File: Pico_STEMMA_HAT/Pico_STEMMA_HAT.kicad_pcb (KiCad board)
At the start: 2 copper layers, 58 x 63 mm, 38 parts

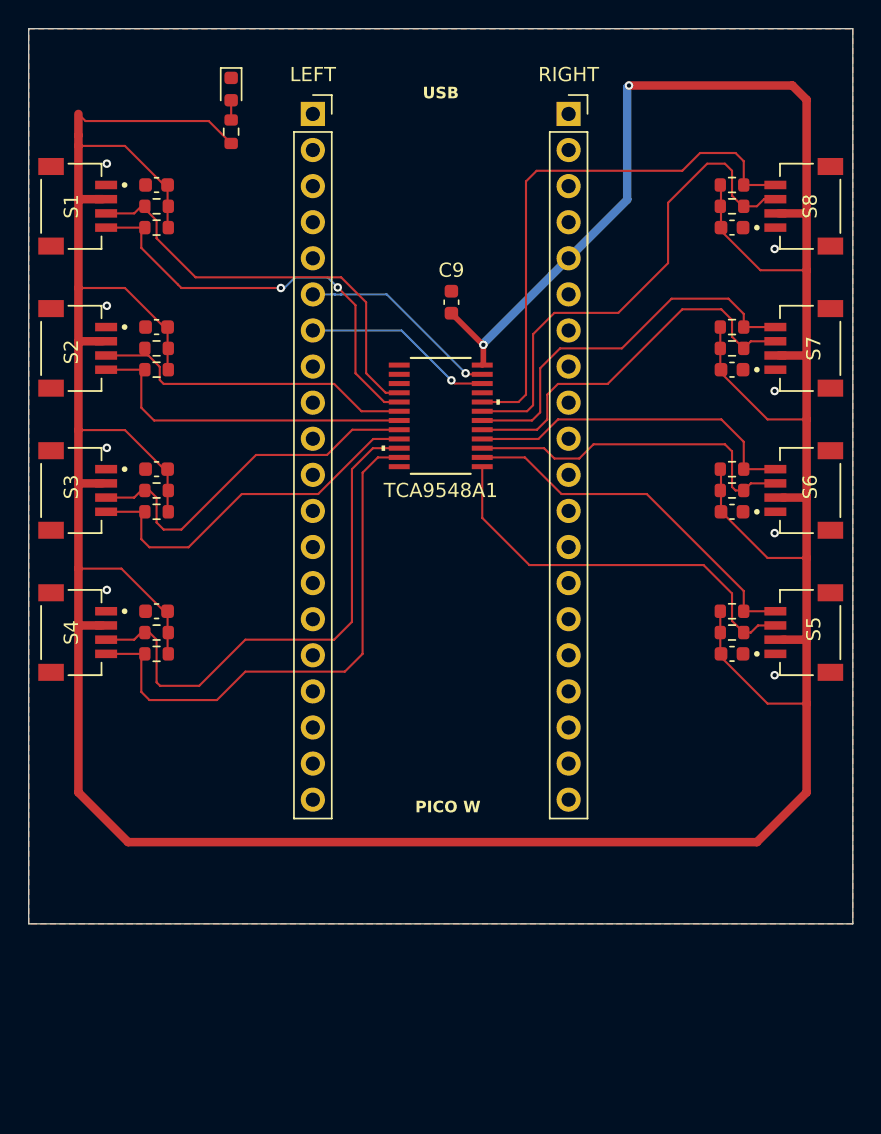
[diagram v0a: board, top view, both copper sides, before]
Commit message: Add GND vias to connect to GND B layer
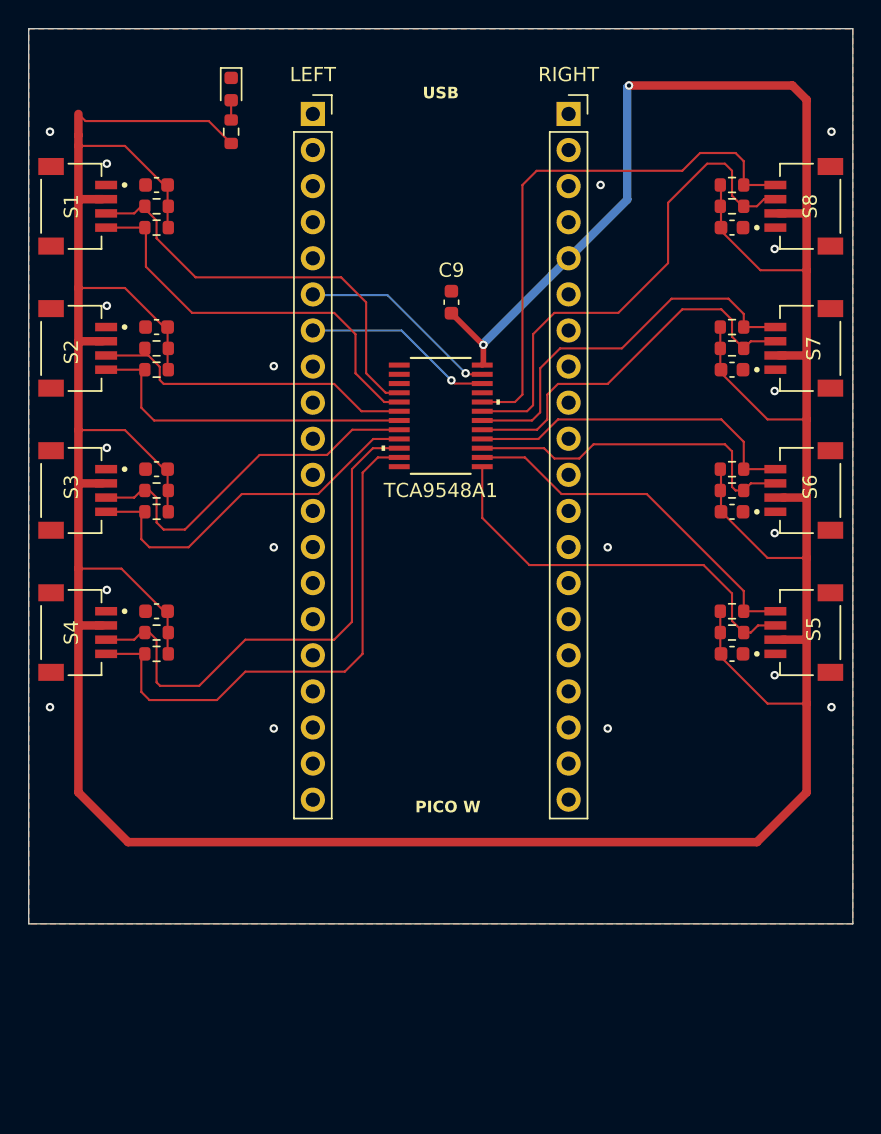
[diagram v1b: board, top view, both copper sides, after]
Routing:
- net /SCL0: track 30.3 -> 29.2 mm, vias 2 -> 0
- net GND: vias 8 -> 18

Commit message: Add SD card reader to PCB design
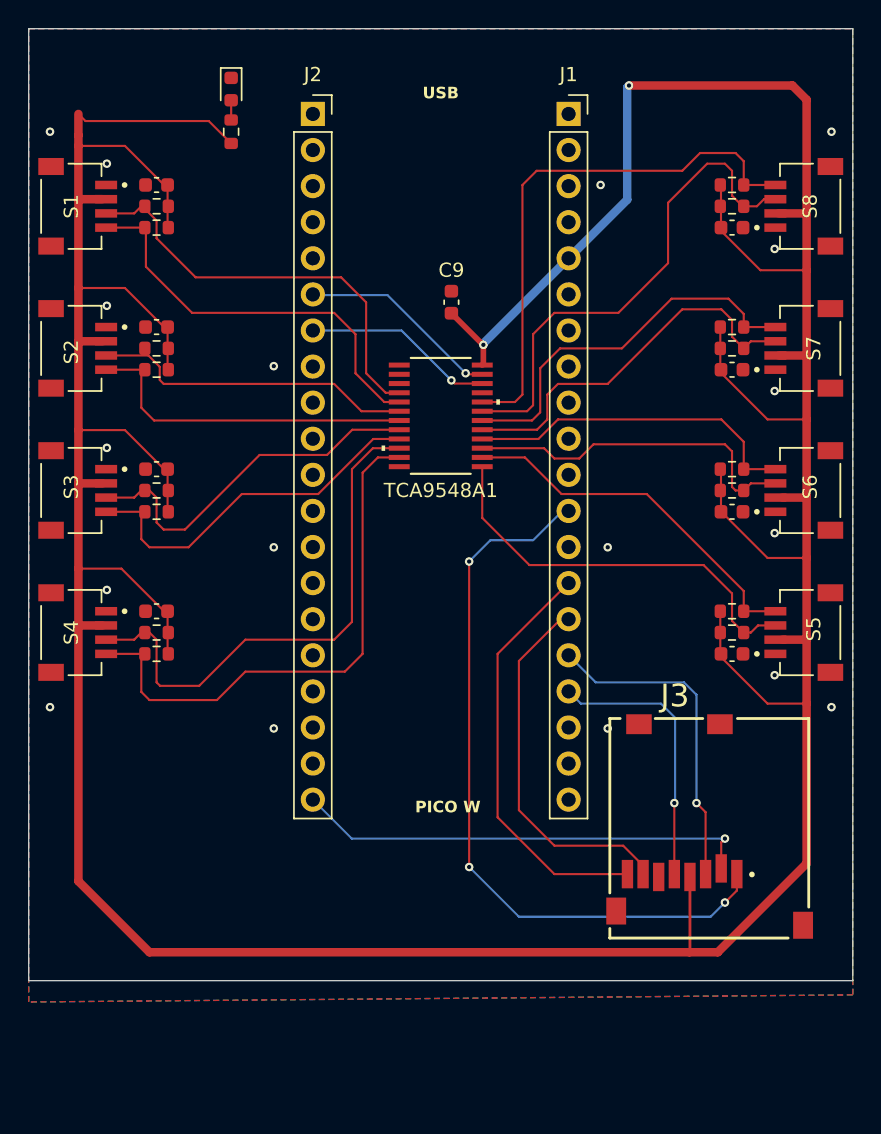
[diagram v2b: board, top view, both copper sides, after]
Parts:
- added J3: SDCARD_MODULE, Pico_Footprints:SDCARD_MODULE_Footprint, F.Cu at (168.9, 128.8)
- renumbered RIGHT to J1, LEFT to J2
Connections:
- net /GPIO16 renamed /GPIO16/DEC
- J1 pad 12: /GPIO22 -> /GPIO22/DAT2
- J1 pad 14: /GPIO21 -> /GPIO21/DAT1
- J1 pad 15: /GPIO20 -> /GPIO20/MISO
- J1 pad 16: /GPIO19 -> /GPIO19/DATA_IN
- J1 pad 17: /GPIO18 -> /GPIO18/SD_CLK
- J2 pad 20: /GPIO15 -> /GPIO15/CS
- S1 pad S1: GND -> (no net)
- S1 pad S2: GND -> (no net)
- S2 pad S1: GND -> (no net)
- S2 pad S2: GND -> (no net)
- S3 pad S1: GND -> (no net)
- S3 pad S2: GND -> (no net)
- S4 pad S1: GND -> (no net)
- S4 pad S2: GND -> (no net)
- S5 pad S1: GND -> (no net)
- S5 pad S2: GND -> (no net)
- S6 pad S1: GND -> (no net)
- S6 pad S2: GND -> (no net)
- S7 pad S1: GND -> (no net)
- S7 pad S2: GND -> (no net)
- S8 pad S1: GND -> (no net)
- S8 pad S2: GND -> (no net)
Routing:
- net /GPIO22/DAT2: track 0.00 -> 52.2 mm, vias 0 -> 3
- net /GPIO15/CS: track 0.00 -> 32.3 mm, vias 0 -> 1
- net /GPIO21/DAT1: track 0.00 -> 29.4 mm
- net /GPIO20/MISO: track 0.00 -> 26.2 mm
- net /GPIO19/DATA_IN: track 0.00 -> 23.0 mm, vias 0 -> 1
- net /GPIO18/SD_CLK: track 0.00 -> 19.3 mm, vias 0 -> 1
- net +3V3: track 299.3 -> 317.6 mm
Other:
- board size 58 x 63 mm -> 58 x 67 mm

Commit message: Add pullup resistors to the SD card reader
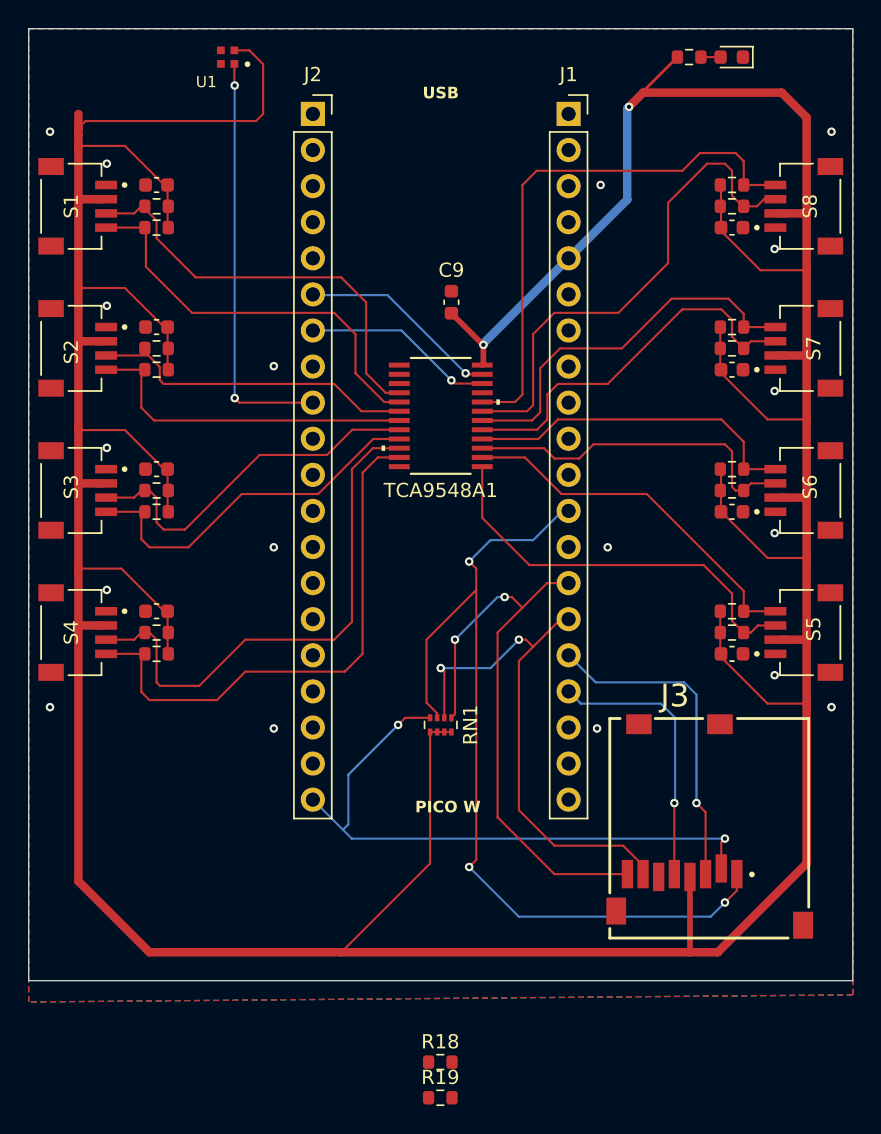
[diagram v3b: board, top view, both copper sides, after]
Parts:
- added R18: 47k, Resistor_SMD:R_0603_1608Metric, F.Cu at (150.0, 145.2)
- added R19: 47k, Resistor_SMD:R_0603_1608Metric, F.Cu at (150.0, 147.7)
- added RN1: 47k, Resistor_SMD:R_Array_Concave_4x0402, F.Cu at (150.0, 121.5)
- added U1: Neopixel, Pico_Footprints:NEOPIXEL_Footprint, F.Cu at (135.0, 74.5)
- moved D1 35.3 mm to (170.5, 74.5), turned to 180 degrees
- moved R17 32.7 mm to (167.5, 74.5), turned to 0 degrees
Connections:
- J2 pad 9: /GPIO6 -> /GPIO6/NEOPIXEL
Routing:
- net /GPIO6/NEOPIXEL: track 0.00 -> 29.2 mm, vias 0 -> 2
- net +3V3: track 317.6 -> 346.4 mm
- net /GPIO21/DAT1: track 29.4 -> 42.1 mm, vias 0 -> 2
- net /GPIO15/CS: track 32.3 -> 43.8 mm, vias 1 -> 2
- net /GPIO22/DAT2: track 52.2 -> 63.4 mm
- net /GPIO20/MISO: track 26.2 -> 37.3 mm, vias 0 -> 2

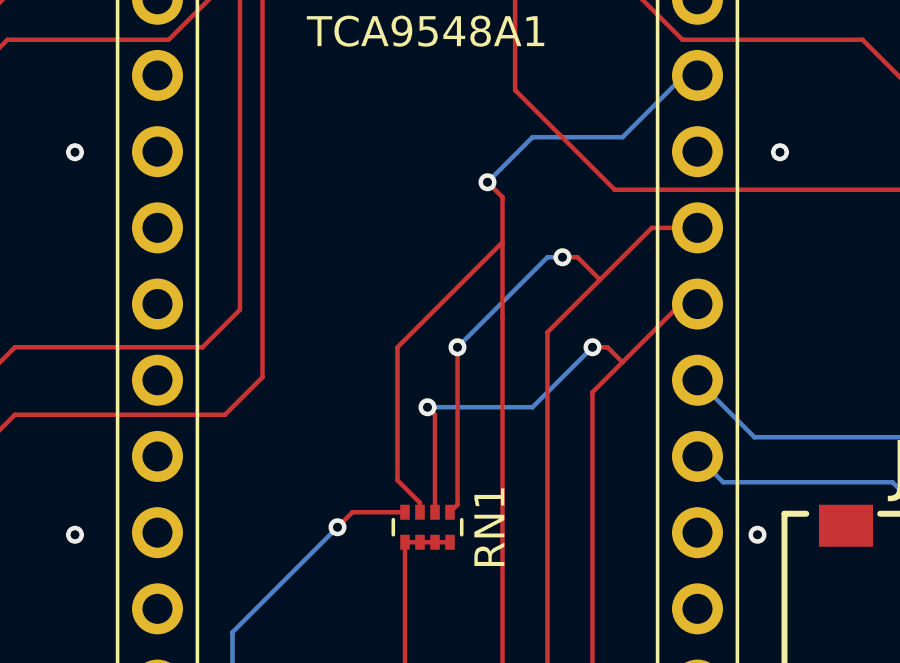
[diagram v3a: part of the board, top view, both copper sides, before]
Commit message: Adjust traces
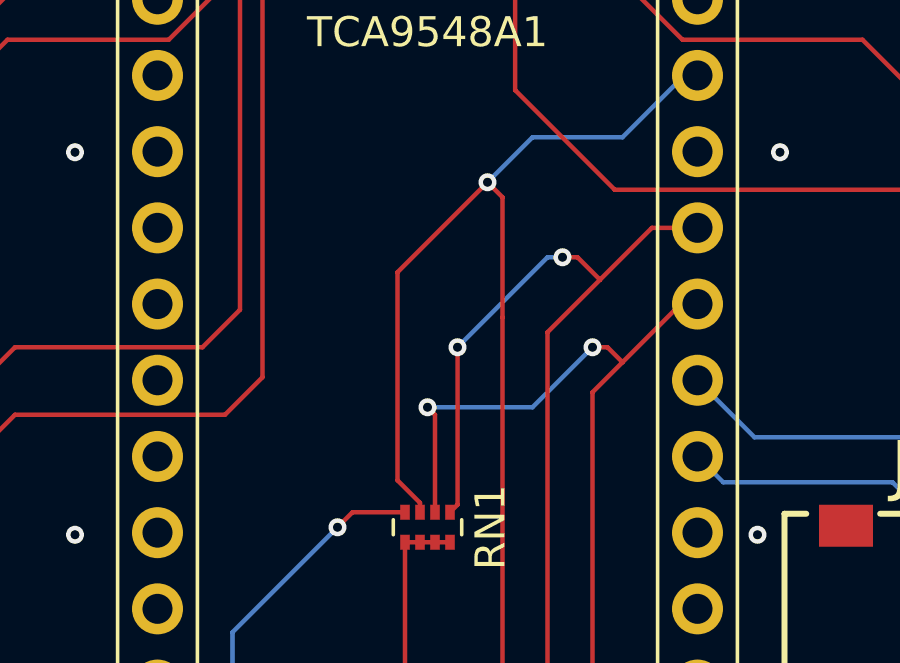
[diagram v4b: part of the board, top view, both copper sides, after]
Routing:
- net /GPIO22/DAT2: track 63.4 -> 65.2 mm
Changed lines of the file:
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@@
 	)
 	(segment
-		(start 149 115.5)
+		(start 149 113)
 		(end 149 119.936)
 		(width 0.15)
@@
 	)
 	(segment
-		(start 152.5 131)
-		(end 152 131.5)
+		(start 149 119.936)
+		(end 149.75 120.686)
 		(width 0.15)
 		(layer "F.Cu")
@@
 	)
 	(segment
-		(start 152.5 112)
-		(end 149 115.5)
+		(start 152.5 131)
+		(end 152 131.5)
 		(width 0.15)
 		(layer "F.Cu")
@@
 	)
 	(segment
-		(start 149 119.936)
-		(end 149.75 120.686)
+		(start 152 110)
+		(end 149 113)
 		(width 0.15)
 		(layer "F.Cu")

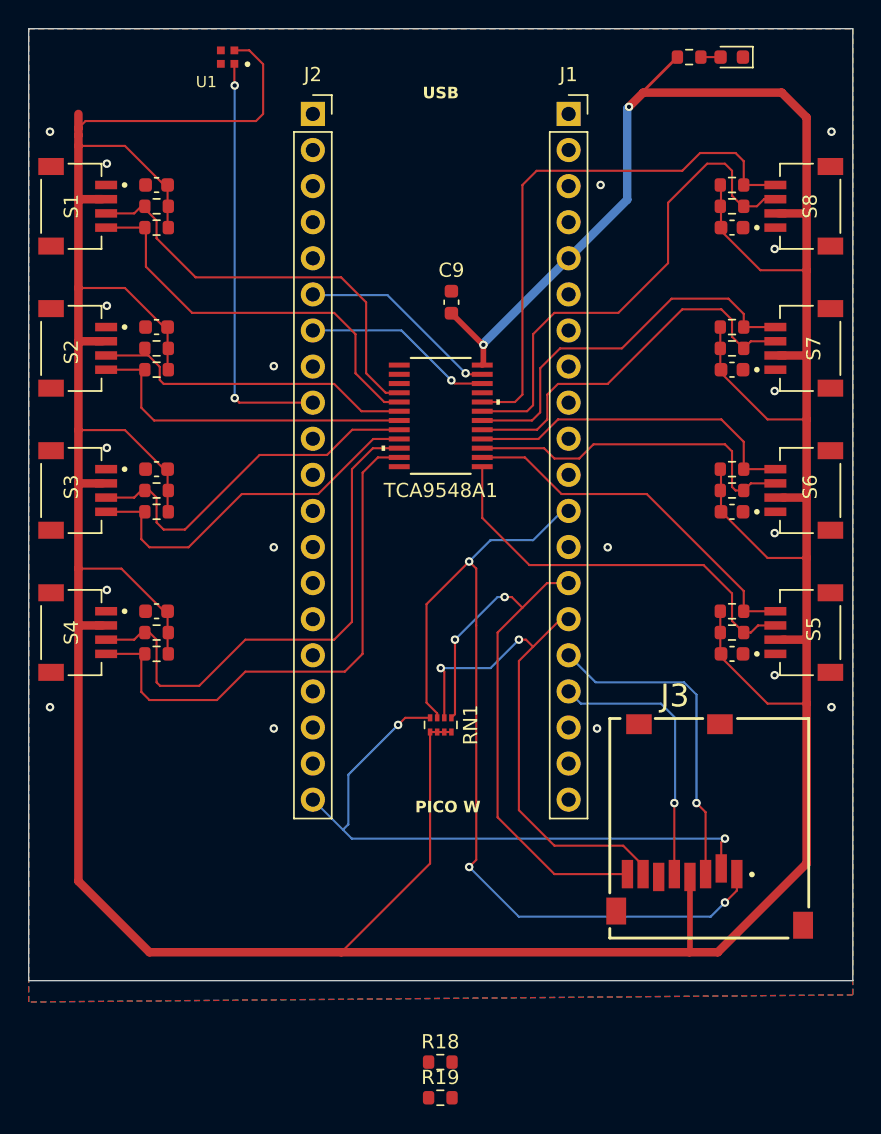
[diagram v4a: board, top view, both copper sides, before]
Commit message: Change pullup resistors
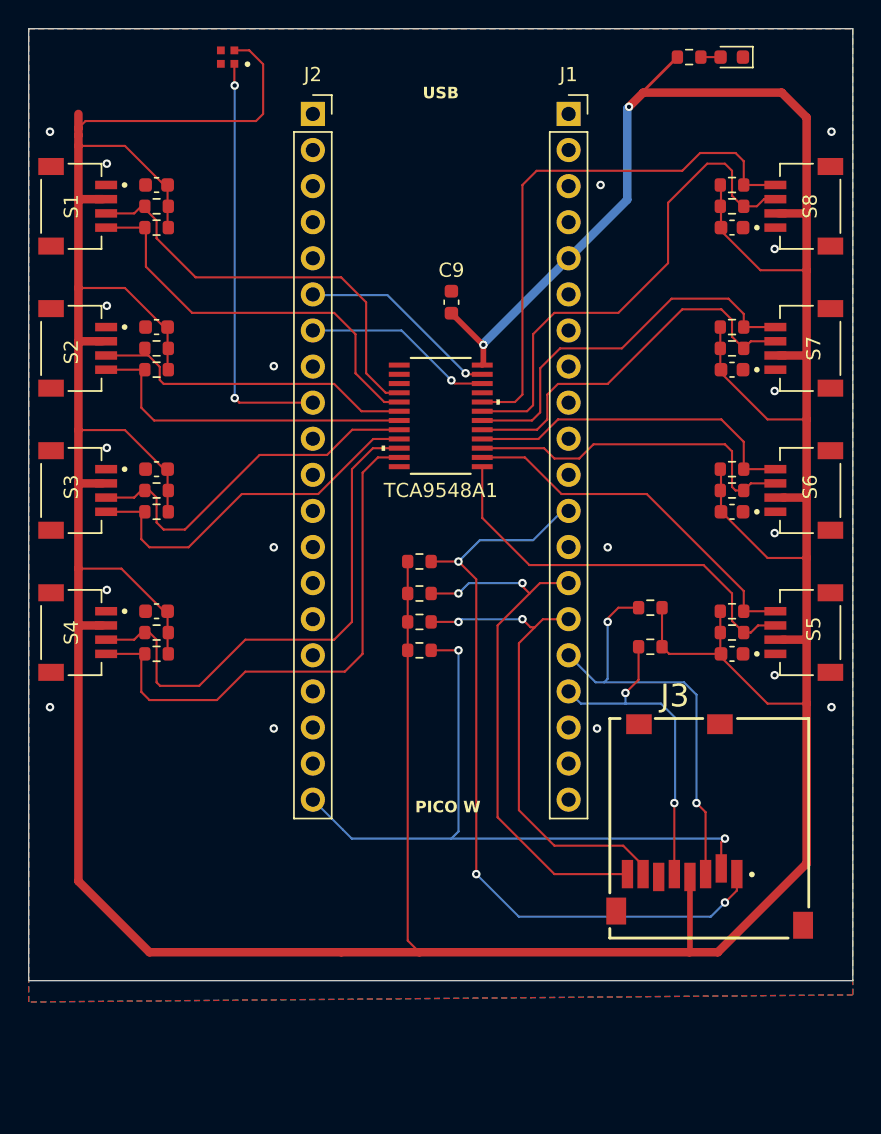
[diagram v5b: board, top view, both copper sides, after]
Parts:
- removed RN1: 47k, Resistor_SMD:R_Array_Concave_4x0402
- added R20: 47k, Resistor_SMD:R_0603_1608Metric, F.Cu at (148.5, 116.2)
- added R21: 47k, Resistor_SMD:R_0603_1608Metric, F.Cu at (148.5, 110.0)
- added R22: 47k, Resistor_SMD:R_0603_1608Metric, F.Cu at (148.5, 112.2)
- added R23: 47k, Resistor_SMD:R_0603_1608Metric, F.Cu at (148.5, 114.2)
- moved R18 35.2 mm to (164.8, 113.2), turned to 180 degrees
- moved R19 35.0 mm to (164.8, 116.0), turned to 180 degrees
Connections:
- R18 pad 1: /GPIO19/DATA_IN -> +3V3
- R18 pad 2: +3V3 -> /GPIO19/DATA_IN
- R19 pad 1: /GPIO18/SD_CLK -> +3V3
- R19 pad 2: +3V3 -> /GPIO18/SD_CLK
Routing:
- net +3V3: track 346.4 -> 361.8 mm
- net /GPIO22/DAT2: track 65.2 -> 55.2 mm
- net /GPIO19/DATA_IN: track 23.0 -> 30.1 mm, vias 1 -> 2
- net /GPIO18/SD_CLK: track 19.3 -> 23.7 mm, vias 1 -> 2
- net /GPIO21/DAT1: track 42.1 -> 38.2 mm
- net /GPIO15/CS: track 43.8 -> 47.7 mm
- net /GPIO20/MISO: track 37.3 -> 34.5 mm
